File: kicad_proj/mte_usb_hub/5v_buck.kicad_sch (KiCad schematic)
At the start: 21 parts

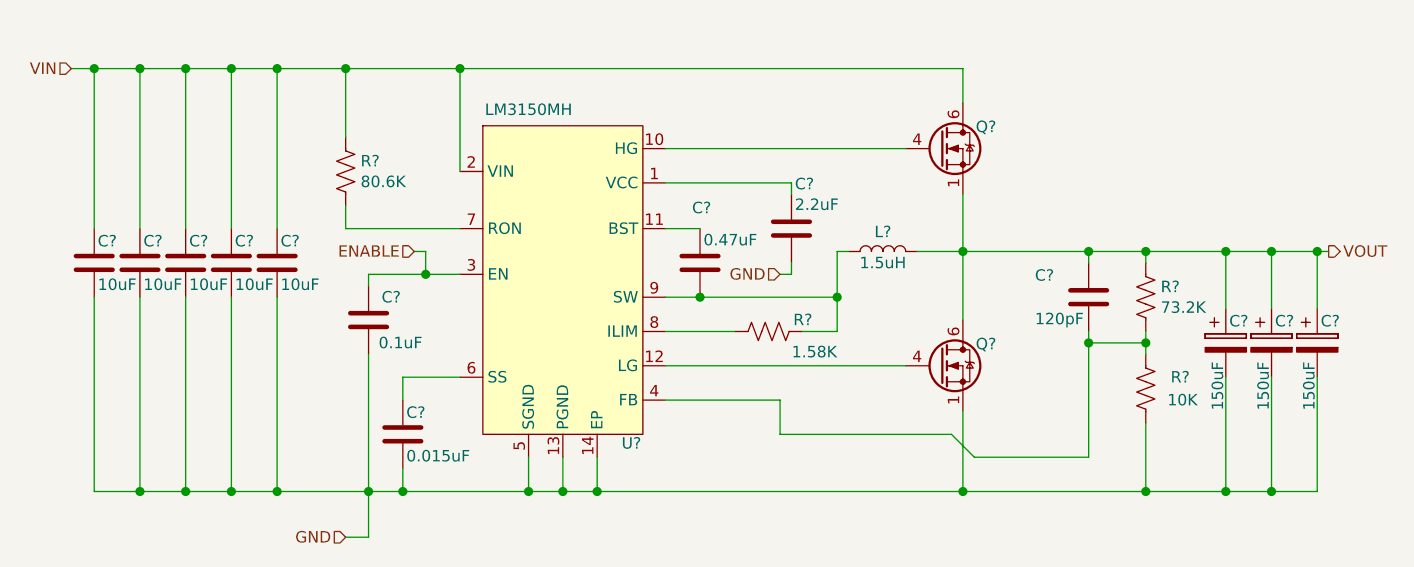
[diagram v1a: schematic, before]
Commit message: Finishes input filter, minor buck changes
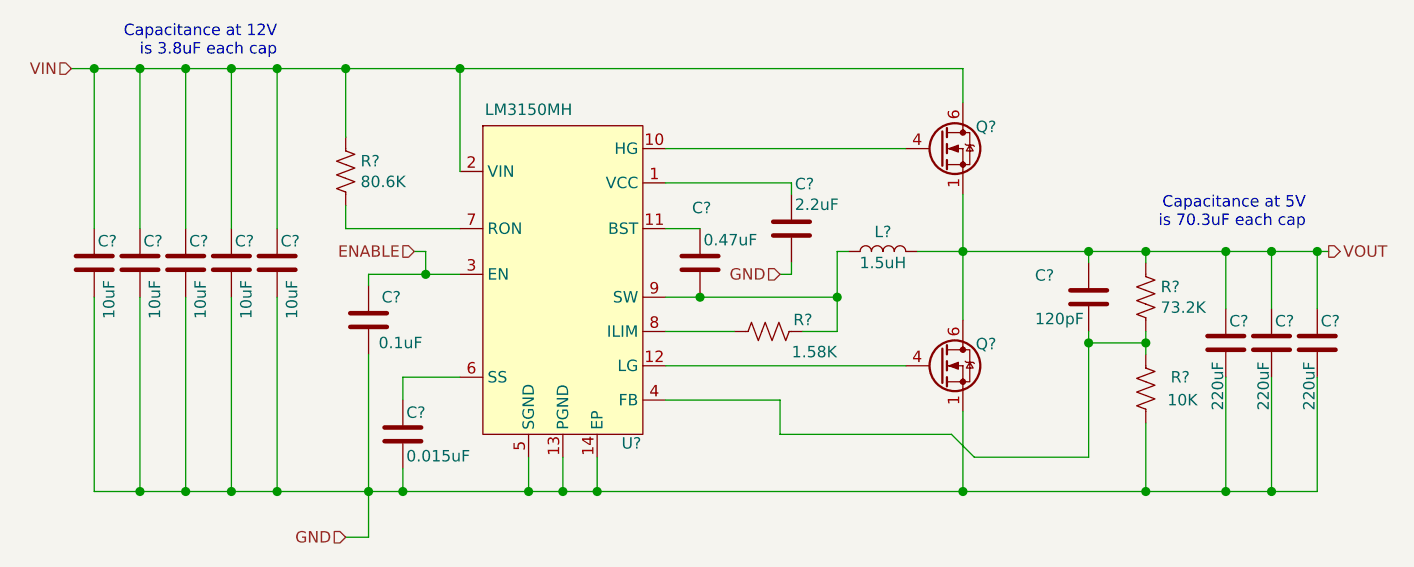
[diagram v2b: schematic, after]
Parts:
- removed C? (x5): C1608X5R1E106M080AC, footprints:CAPACITOR_0603N, symbol mte_usb_hub:C1608X5R1E106M080AC
- removed C? (x3): APXE100ARA151MF80G, symbol mte_usb_hub:APXE100ARA151MF80G
- added C? (x3): GRM32ER60J227ME05L, footprints:CAPACITOR_1210N, symbol mte_usb_hub:GRM32ER60J227ME05L
- added C? (x5): GRM31CR71E106KA12L, footprints:CAPACITOR_1206N, symbol mte_usb_hub:GRM31CR71E106KA12L
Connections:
- net GND: now also C?.2, C?.2, C?.2, C?.2, C?.2, C?.2, C?.2, C?.2
- net VIN: now also C?.1, C?.1, C?.1, C?.1, C?.1
- net VOUT: now also C?.1, C?.1, C?.1
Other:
- note added: "Capacitance at 12V is 3.8uF each cap"
- note added: "Capacitance at 5V is 70.3uF each cap"

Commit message: Updates input protection, output BC enabled
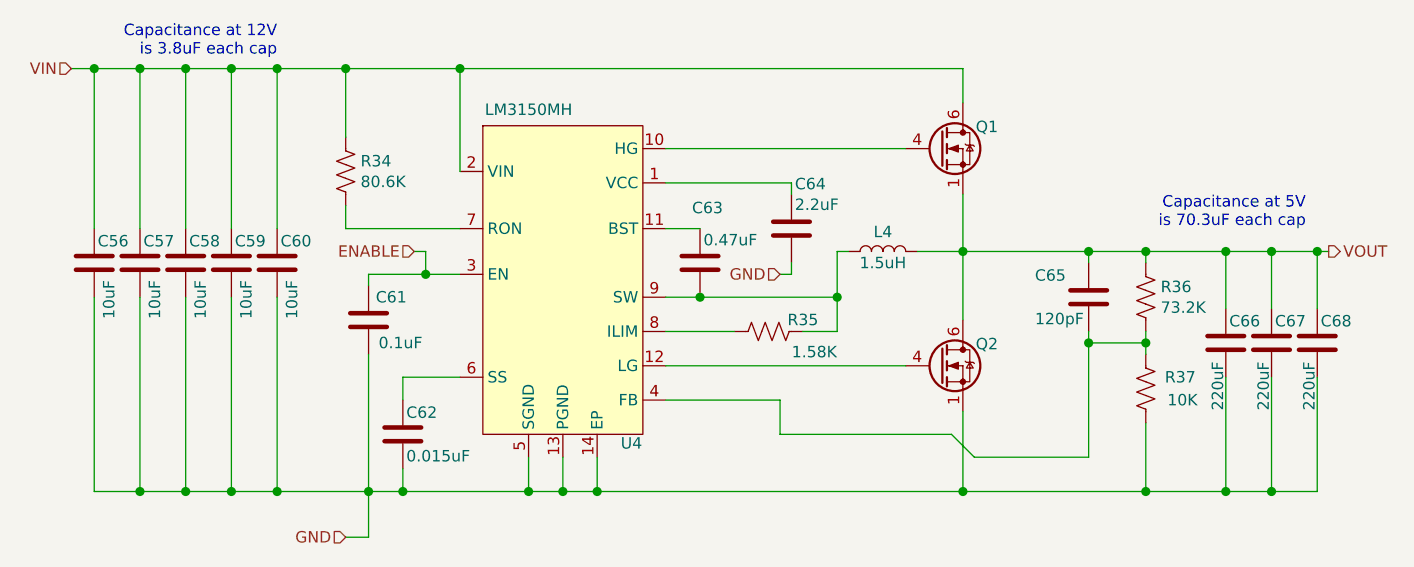
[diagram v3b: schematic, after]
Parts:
- gave numbers to parts that had none: 21
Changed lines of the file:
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@@
-(kicad_sch (version 20210126) (generator eeschema)
+(kicad_sch (version 20210406) (generator eeschema)
   (paper "A4")
   (junction (at 39.37 53.34) (diameter 1.016) (color 0 0 0 0))
@@
   (symbol (lib_id "Device:L") (at 127 73.66 90) (unit 1)
     (in_bom yes) (on_board yes)
-    (property "Reference" "L?" (id 0) (at 127 71.4818 90))
+    (property "Reference" "L4" (id 0) (at 127 71.4818 90))
     (property "Value" "SRP1270-1R5M" (id 1) (at 127 75.0505 90)
       (effects (font (size 1.27 1.27)) hide)
@@
   (symbol (lib_id "mte_usb_hub:RC0402FR-0780K6L") (at 67.31 64.77 0) (unit 1)
     (in_bom yes) (on_board yes)
-    (property "Reference" "R?" (id 0) (at 68.9611 63.6206 0)
+    (property "Reference" "R34" (id 0) (at 68.9611 63.6206 0)
       (effects (font (size 1.27 1.27)) (justify left))
     )
@@
   (symbol (lib_id "mte_usb_hub:RC0402FR-071K58L") (at 114.3 82.55 90) (unit 1)
     (in_bom yes) (on_board yes)
-    (property "Reference" "R?" (id 0) (at 118.11 81.2608 90))
+    (property "Reference" "R35" (id 0) (at 118.11 81.2608 90))
     (property "Value" "RC0402FR-071K58L" (id 1) (at 114.3 85.09 90)
       (effects (font (size 1.27 1.27)) hide)
@@
   (symbol (lib_id "mte_usb_hub:RC0402FR-0773K2L") (at 156.21 78.74 0) (unit 1)
     (in_bom yes) (on_board yes)
-    (property "Reference" "R?" (id 0) (at 157.8611 77.5906 0)
+    (property "Reference" "R36" (id 0) (at 157.8611 77.5906 0)
       (effects (font (size 1.27 1.27)) (justify left))
     )
@@
   (symbol (lib_id "mte_usb_hub:RC0402JR-0710KL") (at 156.21 88.9 0) (unit 1)
     (in_bom yes) (on_board yes)
-    (property "Reference" "R?" (id 0) (at 160.0392 87.63 0))
+    (property "Reference" "R37" (id 0) (at 160.0392 87.63 0))
     (property "Value" "RC0402JR-0710KL" (id 1) (at 153.67 88.9 90)
       (effects (font (size 1.27 1.27)) hide)
@@
   (symbol (lib_id "mte_usb_hub:GRM31CR71E106KA12L") (at 39.37 74.93 0) (unit 1)
     (in_bom yes) (on_board yes)
-    (property "Reference" "C?" (id 0) (at 39.7511 72.5106 0)
+    (property "Reference" "C56" (id 0) (at 39.7511 72.5106 0)
       (effects (font (size 1.27 1.27)) (justify left))
     )
@@
   (symbol (lib_id "mte_usb_hub:GRM31CR71E106KA12L") (at 44.45 74.93 0) (unit 1)
     (in_bom yes) (on_board yes)
-    (property "Reference" "C?" (id 0) (at 44.8311 72.5106 0)
+    (property "Reference" "C57" (id 0) (at 44.8311 72.5106 0)
       (effects (font (size 1.27 1.27)) (justify left))
     )
@@
   (symbol (lib_id "mte_usb_hub:GRM31CR71E106KA12L") (at 49.53 74.93 0) (unit 1)
     (in_bom yes) (on_board yes)
-    (property "Reference" "C?" (id 0) (at 49.9111 72.5106 0)
+    (property "Reference" "C58" (id 0) (at 49.9111 72.5106 0)
       (effects (font (size 1.27 1.27)) (justify left))
     )
@@
   (symbol (lib_id "mte_usb_hub:GRM31CR71E106KA12L") (at 54.61 74.93 0) (unit 1)
     (in_bom yes) (on_board yes)
-    (property "Reference" "C?" (id 0) (at 54.9911 72.5106 0)
+    (property "Reference" "C59" (id 0) (at 54.9911 72.5106 0)
       (effects (font (size 1.27 1.27)) (justify left))
     )
@@
   (symbol (lib_id "mte_usb_hub:GRM31CR71E106KA12L") (at 59.69 74.93 0) (unit 1)
     (in_bom yes) (on_board yes)
-    (property "Reference" "C?" (id 0) (at 60.0711 72.5106 0)
+    (property "Reference" "C60" (id 0) (at 60.0711 72.5106 0)
       (effects (font (size 1.27 1.27)) (justify left))
     )
@@
   (symbol (lib_id "mte_usb_hub:CC0402KRX5R7BB104") (at 69.85 81.28 180) (unit 1)
     (in_bom yes) (on_board yes)
-    (property "Reference" "C?" (id 0) (at 72.3708 78.74 0))
+    (property "Reference" "C61" (id 0) (at 72.3708 78.74 0))
     (property "Value" "CC0402KRX5R7BB104" (id 1) (at 69.215 78.74 0)
       (effects (font (size 1.27 1.27)) (justify left) hide)
@@
   (symbol (lib_id "mte_usb_hub:TMK105BJ153KV-F") (at 73.66 93.98 0) (unit 1)
     (in_bom yes) (on_board yes)
-    (property "Reference" "C?" (id 0) (at 74.0411 91.5606 0)
+    (property "Reference" "C62" (id 0) (at 74.0411 91.5606 0)
       (effects (font (size 1.27 1.27)) (justify left))
     )
@@
   (symbol (lib_id "mte_usb_hub:TMK105ABJ474KV-F") (at 106.68 74.93 0) (unit 1)
     (in_bom yes) (on_board yes)
-    (property "Reference" "C?" (id 0) (at 105.7911 68.8213 0)
+    (property "Reference" "C63" (id 0) (at 105.7911 68.8213 0)
       (effects (font (size 1.27 1.27)) (justify left))
     )
@@
   (symbol (lib_id "mte_usb_hub:TMK105CBJ225MV-F") (at 116.84 71.12 0) (unit 1)
     (in_bom yes) (on_board yes)
-    (property "Reference" "C?" (id 0) (at 117.2211 66.1606 0)
+    (property "Reference" "C64" (id 0) (at 117.2211 66.1606 0)
       (effects (font (size 1.27 1.27)) (justify left))
     )
@@
   (symbol (lib_id "mte_usb_hub:C0402C121J3GAC7867") (at 149.86 78.74 0) (unit 1)
     (in_bom yes) (on_board yes)
-    (property "Reference" "C?" (id 0) (at 143.8911 76.3206 0)
+    (property "Reference" "C65" (id 0) (at 143.8911 76.3206 0)
       (effects (font (size 1.27 1.27)) (justify left))
     )
@@
   (symbol (lib_id "mte_usb_hub:GRM32ER60J227ME05L") (at 165.1 83.82 0) (unit 1)
     (in_bom yes) (on_board yes)
-    (property "Reference" "C?" (id 0) (at 165.4811 81.4006 0)
+    (property "Reference" "C66" (id 0) (at 165.4811 81.4006 0)
       (effects (font (size 1.27 1.27)) (justify left))
     )
@@
   (symbol (lib_id "mte_usb_hub:GRM32ER60J227ME05L") (at 170.18 83.82 0) (unit 1)
     (in_bom yes) (on_board yes)
-    (property "Reference" "C?" (id 0) (at 170.5611 81.4006 0)
+    (property "Reference" "C67" (id 0) (at 170.5611 81.4006 0)
       (effects (font (size 1.27 1.27)) (justify left))
     )
@@
   (symbol (lib_id "mte_usb_hub:GRM32ER60J227ME05L") (at 175.26 83.82 0) (unit 1)
     (in_bom yes) (on_board yes)
-    (property "Reference" "C?" (id 0) (at 175.6411 81.4006 0)
+    (property "Reference" "C68" (id 0) (at 175.6411 81.4006 0)
       (effects (font (size 1.27 1.27)) (justify left))
     )
@@
   (symbol (lib_id "mte_usb_hub:CSD16342Q5A") (at 135.89 62.23 0) (unit 1)
     (in_bom yes) (on_board yes)
-    (property "Reference" "Q?" (id 0) (at 137.3125 59.8106 0)
+    (property "Reference" "Q1" (id 0) (at 137.3125 59.8106 0)
       (effects (font (size 1.27 1.27)) (justify left))
     )
@@
   (symbol (lib_id "mte_usb_hub:CSD17577Q5AT") (at 135.89 86.36 0) (unit 1)
     (in_bom yes) (on_board yes)
-    (property "Reference" "Q?" (id 0) (at 137.3125 83.9406 0)
+    (property "Reference" "Q2" (id 0) (at 137.3125 83.9406 0)
       (effects (font (size 1.27 1.27)) (justify left))
     )
@@
   (symbol (lib_id "mte_usb_hub:LM3150MH") (at 91.44 76.2 0) (unit 1)
     (in_bom yes) (on_board yes)
-    (property "Reference" "U?" (id 0) (at 99.06 94.9763 0))
+    (property "Reference" "U4" (id 0) (at 99.06 94.9763 0))
     (property "Value" "LM3150MH" (id 1) (at 87.63 57.905 0))
     (property "Footprint" "" (id 2) (at 111.76 30.48 0)

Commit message: New changes from the livestream
Starts the layout
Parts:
- C56, C57, C58, C59, C60: footprint footprints:CAPACITOR_1206N -> mte_usb_footprints:CAPACITOR_1206N
- C61, C62, C63, C64, C65: footprint footprints:CAPACITOR_0402N -> mte_usb_footprints:CAPACITOR_0402N
- C66, C67, C68: footprint footprints:CAPACITOR_1210N -> mte_usb_footprints:CAPACITOR_1210N
- L4: footprint (none) -> mte_usb_footprints:INDM1350X1350X700L250X300N
- Q1, Q2: footprint (none) -> mte_usb_footprints:CSD16342Q5A
- R34, R35, R36, R37: footprint footprints:RESISTOR_0402N -> mte_usb_footprints:RESISTOR_0402N
- U4: footprint (none) -> mte_usb_footprints:SOP15P65_500X640X110L60X24T310X300N
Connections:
- net GND: now also U4.15 (EP), U4.9 (SGND); no longer U4.13 (PGND)
- net at C63.1: now also U4.12 (BST); no longer U4.11 (BST)
- net at C63.2, L4.1, R35.2: now also U4.10 (SW); no longer U4.9 (SW)
- net at Q1.4 (G): now also U4.11 (HG); no longer U4.10 (HG)
- net at Q2.4 (G): now also U4.13 (LG); no longer U4.12 (LG)
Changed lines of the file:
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@@
   (junction (at 76.2 76.2) (diameter 1.016) (color 0 0 0 0))
   (junction (at 80.01 53.34) (diameter 1.016) (color 0 0 0 0))
-  (junction (at 87.63 100.33) (diameter 1.016) (color 0 0 0 0))
-  (junction (at 91.44 100.33) (diameter 1.016) (color 0 0 0 0))
-  (junction (at 95.25 100.33) (diameter 1.016) (color 0 0 0 0))
+  (junction (at 86.36 100.33) (diameter 1.016) (color 0 0 0 0))
+  (junction (at 88.9 100.33) (diameter 1.016) (color 0 0 0 0))
+  (junction (at 92.71 100.33) (diameter 1.016) (color 0 0 0 0))
+  (junction (at 96.52 100.33) (diameter 1.016) (color 0 0 0 0))
   (junction (at 106.68 78.74) (diameter 1.016) (color 0 0 0 0))
   (junction (at 121.92 78.74) (diameter 1.016) (color 0 0 0 0))
@@
     (stroke (width 0) (type solid) (color 0 0 0 0))
   )
-  (wire (pts (xy 73.66 100.33) (xy 87.63 100.33))
+  (wire (pts (xy 73.66 100.33) (xy 86.36 100.33))
     (stroke (width 0) (type solid) (color 0 0 0 0))
   )
@@
     (stroke (width 0) (type solid) (color 0 0 0 0))
   )
-  (wire (pts (xy 87.63 96.52) (xy 87.63 100.33))
-    (stroke (width 0) (type solid) (color 0 0 0 0))
-  )
-  (wire (pts (xy 87.63 100.33) (xy 91.44 100.33))
-    (stroke (width 0) (type solid) (color 0 0 0 0))
-  )
-  (wire (pts (xy 91.44 100.33) (xy 91.44 96.52))
-    (stroke (width 0) (type solid) (color 0 0 0 0))
-  )
-  (wire (pts (xy 95.25 96.52) (xy 95.25 100.33))
-    (stroke (width 0) (type solid) (color 0 0 0 0))
-  )
-  (wire (pts (xy 95.25 100.33) (xy 91.44 100.33))
+  (wire (pts (xy 86.36 96.52) (xy 86.36 100.33))
+    (stroke (width 0) (type solid) (color 0 0 0 0))
+  )
+  (wire (pts (xy 86.36 100.33) (xy 88.9 100.33))
+    (stroke (width 0) (type solid) (color 0 0 0 0))
+  )
+  (wire (pts (xy 88.9 100.33) (xy 88.9 96.52))
+    (stroke (width 0) (type solid) (color 0 0 0 0))
+  )
+  (wire (pts (xy 88.9 100.33) (xy 92.71 100.33))
+    (stroke (width 0) (type solid) (color 0 0 0 0))
+  )
+  (wire (pts (xy 92.71 96.52) (xy 92.71 100.33))
+    (stroke (width 0) (type solid) (color 0 0 0 0))
+  )
+  (wire (pts (xy 92.71 100.33) (xy 96.52 100.33))
+    (stroke (width 0) (type solid) (color 0 0 0 0))
+  )
+  (wire (pts (xy 96.52 96.52) (xy 96.52 100.33))
+    (stroke (width 0) (type solid) (color 0 0 0 0))
+  )
+  (wire (pts (xy 96.52 100.33) (xy 135.89 100.33))
     (stroke (width 0) (type solid) (color 0 0 0 0))
   )
@@
   )
   (wire (pts (xy 135.89 91.44) (xy 135.89 100.33))
-    (stroke (width 0) (type solid) (color 0 0 0 0))
-  )
-  (wire (pts (xy 135.89 100.33) (xy 95.25 100.33))
     (stroke (width 0) (type solid) (color 0 0 0 0))
   )
@@
       (effects (font (size 1.27 1.27)) hide)
     )
-    (property "Footprint" "" (id 2) (at 127 73.66 0)
+    (property "Footprint" "mte_usb_footprints:INDM1350X1350X700L250X300N" (id 2) (at 127 73.66 0)
       (effects (font (size 1.27 1.27)) hide)
     )
@@
       (effects (font (size 1.27 1.27)) hide)
     )
-    (property "Footprint" "footprints:RESISTOR_0402N" (id 2) (at 68.326 65.024 90)
+    (property "Footprint" "mte_usb_footprints:RESISTOR_0402N" (id 2) (at 68.326 65.024 90)
       (effects (font (size 1.27 1.27)) hide)
     )
@@
       (effects (font (size 1.27 1.27)) hide)
     )
-    (property "Footprint" "footprints:RESISTOR_0402N" (id 2) (at 114.554 81.534 90)
+    (property "Footprint" "mte_usb_footprints:RESISTOR_0402N" (id 2) (at 114.554 81.534 90)
       (effects (font (size 1.27 1.27)) hide)
     )
@@
       (effects (font (size 1.27 1.27)) hide)
     )
-    (property "Footprint" "footprints:RESISTOR_0402N" (id 2) (at 157.226 78.994 90)
+    (property "Footprint" "mte_usb_footprints:RESISTOR_0402N" (id 2) (at 157.226 78.994 90)
       (effects (font (size 1.27 1.27)) hide)
     )
@@
       (effects (font (size 1.27 1.27)) hide)
     )
-    (property "Footprint" "footprints:RESISTOR_0402N" (id 2) (at 157.226 89.154 90)
+    (property "Footprint" "mte_usb_footprints:RESISTOR_0402N" (id 2) (at 157.226 89.154 90)
       (effects (font (size 1.27 1.27)) hide)
     )
@@
       (effects (font (size 1.27 1.27)) (justify left) hide)
     )
-    (property "Footprint" "footprints:CAPACITOR_1206N" (id 2) (at 40.3352 78.74 0)
+    (property "Footprint" "mte_usb_footprints:CAPACITOR_1206N" (id 2) (at 40.3352 78.74 0)
       (effects (font (size 1.27 1.27)) hide)
     )
@@
       (effects (font (size 1.27 1.27)) (justify left) hide)
     )
-    (property "Footprint" "footprints:CAPACITOR_1206N" (id 2) (at 45.4152 78.74 0)
+    (property "Footprint" "mte_usb_footprints:CAPACITOR_1206N" (id 2) (at 45.4152 78.74 0)
       (effects (font (size 1.27 1.27)) hide)
     )
@@
       (effects (font (size 1.27 1.27)) (justify left) hide)
     )
-    (property "Footprint" "footprints:CAPACITOR_1206N" (id 2) (at 50.4952 78.74 0)
+    (property "Footprint" "mte_usb_footprints:CAPACITOR_1206N" (id 2) (at 50.4952 78.74 0)
       (effects (font (size 1.27 1.27)) hide)
     )
@@
       (effects (font (size 1.27 1.27)) (justify left) hide)
     )
-    (property "Footprint" "footprints:CAPACITOR_1206N" (id 2) (at 55.5752 78.74 0)
+    (property "Footprint" "mte_usb_footprints:CAPACITOR_1206N" (id 2) (at 55.5752 78.74 0)
       (effects (font (size 1.27 1.27)) hide)
     )
@@
       (effects (font (size 1.27 1.27)) (justify left) hide)
     )
-    (property "Footprint" "footprints:CAPACITOR_1206N" (id 2) (at 60.6552 78.74 0)
+    (property "Footprint" "mte_usb_footprints:CAPACITOR_1206N" (id 2) (at 60.6552 78.74 0)
       (effects (font (size 1.27 1.27)) hide)
     )
@@
       (effects (font (size 1.27 1.27)) (justify left) hide)
     )
-    (property "Footprint" "footprints:CAPACITOR_0402N" (id 2) (at 68.8848 77.47 0)
+    (property "Footprint" "mte_usb_footprints:CAPACITOR_0402N" (id 2) (at 68.8848 77.47 0)
       (effects (font (size 1.27 1.27)) hide)
     )
@@
       (effects (font (size 1.27 1.27)) (justify left) hide)
     )
-    (property "Footprint" "footprints:CAPACITOR_0402N" (id 2) (at 74.6252 97.79 0)
+    (property "Footprint" "mte_usb_footprints:CAPACITOR_0402N" (id 2) (at 74.6252 97.79 0)
       (effects (font (size 1.27 1.27)) hide)
     )
@@
       (effects (font (size 1.27 1.27)) (justify left) hide)
     )
-    (property "Footprint" "footprints:CAPACITOR_0402N" (id 2) (at 107.6452 78.74 0)
+    (property "Footprint" "mte_usb_footprints:CAPACITOR_0402N" (id 2) (at 107.6452 78.74 0)
       (effects (font (size 1.27 1.27)) hide)
     )
@@
       (effects (font (size 1.27 1.27)) (justify left) hide)
     )
-    (property "Footprint" "footprints:CAPACITOR_0402N" (id 2) (at 117.8052 74.93 0)
+    (property "Footprint" "mte_usb_footprints:CAPACITOR_0402N" (id 2) (at 117.8052 74.93 0)
       (effects (font (size 1.27 1.27)) hide)
     )
@@
       (effects (font (size 1.27 1.27)) (justify left) hide)
     )
-    (property "Footprint" "footprints:CAPACITOR_0402N" (id 2) (at 150.8252 82.55 0)
+    (property "Footprint" "mte_usb_footprints:CAPACITOR_0402N" (id 2) (at 150.8252 82.55 0)
       (effects (font (size 1.27 1.27)) hide)
     )
@@
       (effects (font (size 1.27 1.27)) (justify left) hide)
     )
-    (property "Footprint" "footprints:CAPACITOR_1210N" (id 2) (at 166.0652 87.63 0)
+    (property "Footprint" "mte_usb_footprints:CAPACITOR_1210N" (id 2) (at 166.0652 87.63 0)
       (effects (font (size 1.27 1.27)) hide)
     )
@@
       (effects (font (size 1.27 1.27)) (justify left) hide)
     )
-    (property "Footprint" "footprints:CAPACITOR_1210N" (id 2) (at 171.1452 87.63 0)
+    (property "Footprint" "mte_usb_footprints:CAPACITOR_1210N" (id 2) (at 171.1452 87.63 0)
       (effects (font (size 1.27 1.27)) hide)
     )
@@
       (effects (font (size 1.27 1.27)) (justify left) hide)
     )
-    (property "Footprint" "footprints:CAPACITOR_1210N" (id 2) (at 176.2252 87.63 0)
+    (property "Footprint" "mte_usb_footprints:CAPACITOR_1210N" (id 2) (at 176.2252 87.63 0)
       (effects (font (size 1.27 1.27)) hide)
     )
@@
       (effects (font (size 1.27 1.27)) (justify left) hide)
     )
-    (property "Footprint" "" (id 2) (at 142.24 48.26 0)
+    (property "Footprint" "mte_usb_footprints:CSD16342Q5A" (id 2) (at 142.24 48.26 0)
       (effects (font (size 1.27 1.27) italic) (justify left) hide)
     )
@@
       (effects (font (size 1.27 1.27)) (justify left) hide)
     )
-    (property "Footprint" "" (id 2) (at 128.27 86.36 0)
+    (property "Footprint" "mte_usb_footprints:CSD16342Q5A" (id 2) (at 128.27 86.36 0)
       (effects (font (size 1.27 1.27) italic) (justify left) hide)
     )
@@
     (property "Reference" "U4" (id 0) (at 99.06 94.9763 0))
     (property "Value" "LM3150MH" (id 1) (at 87.63 57.905 0))
-    (property "Footprint" "" (id 2) (at 111.76 30.48 0)
+    (property "Footprint" "mte_usb_footprints:SOP15P65_500X640X110L60X24T310X300N" (id 2) (at 111.76 30.48 0)
       (effects (font (size 1.27 1.27)) hide)
     )
@@
       (effects (font (size 1.27 1.27)) hide)
     )
-    (pin "1")
     (pin "10")
+    (pin "1")
     (pin "11")
     (pin "12")
     (pin "13")
     (pin "14")
+    (pin "15")
     (pin "2")
     (pin "3")
